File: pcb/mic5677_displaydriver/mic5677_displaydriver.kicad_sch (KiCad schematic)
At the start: 81 parts, among them J1 Segment DIP14, J2 Segment DIP14, J3 Segment Wire Connector, J4 Common Cathode Enable, J5 PSU, J6 Bypass, J7 Serial Debug, J8 8P8C, Q1 D45H8G, Q10 BC546, Q11 BC546, Q12 BC546, Q13 BC546, Q14 BC546, Q15 BC546, Q16 BC546, Q17 BC546, Q18 BC546, Q19 BC546, Q2 D45H8G, Q20 BC546, Q21 BC546, Q22 BC546, Q23 BC546, Q3 D45H8G, Q4 D45H8G, Q5 D45H8G, Q6 D45H8G, Q7 D45H8G, Q8 D45H8G, Q9 D45H8G, U1 L7805, U2 74HC595, U3 74HC595, U4 74HC02

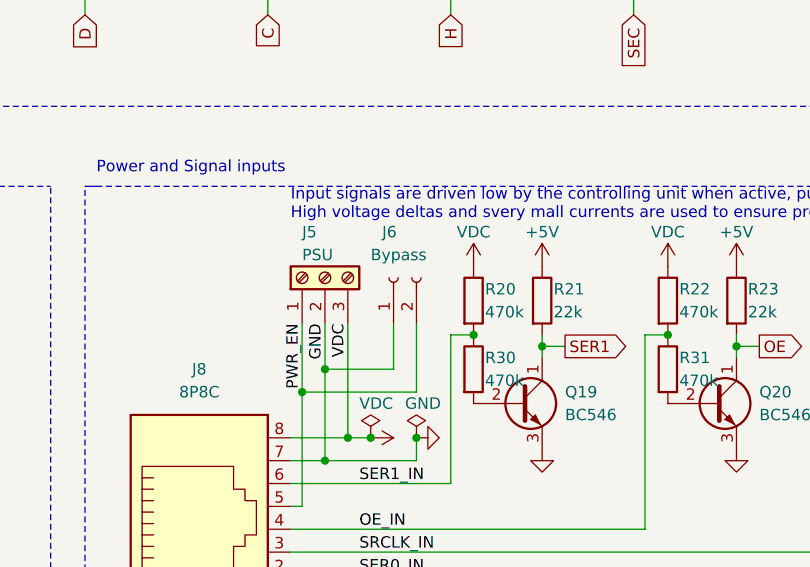
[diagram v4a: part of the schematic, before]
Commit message: Added some silkscreen on pcb and changed io style
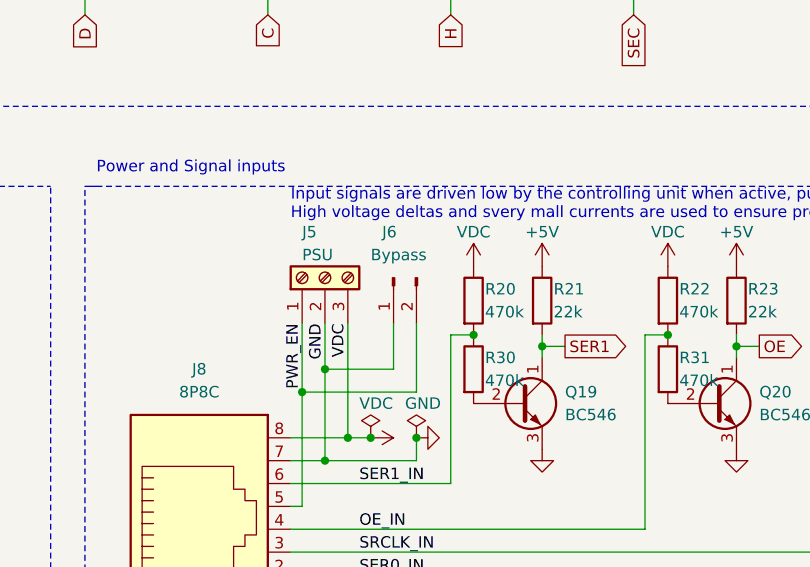
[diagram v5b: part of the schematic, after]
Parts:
- J6: symbol Connector:Conn_01x02_Socket -> Connector:Conn_01x02_Pin
- J7: footprint Connector_PinHeader_2.54mm:PinHeader_1x05_P2.54mm_Vertical -> Connector_PinSocket_2.54mm:PinSocket_1x05_P2.54mm_Vertical
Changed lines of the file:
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@@
       (effects (font (size 1.27 1.27)) (justify left))
     )
-    (property "Footprint" "Connector_PinHeader_2.54mm:PinHeader_1x05_P2.54mm_Vertical" (at 105.41 138.43 0)
+    (property "Footprint" "Connector_PinSocket_2.54mm:PinSocket_1x05_P2.54mm_Vertical" (at 105.41 138.43 0)
       (effects (font (size 1.27 1.27)) hide)
     )
@@
     )
   )
-  (symbol (lib_id "Connector:Conn_01x02_Socket") (at 166.37 114.3 90) (unit 1)
+  (symbol (lib_id "Connector:Conn_01x02_Pin") (at 166.37 114.3 90) (mirror x) (unit 1)
     (in_bom yes) (on_board yes) (dnp no)
     (property "Reference" "J6" (at 165.1 109.22 90)

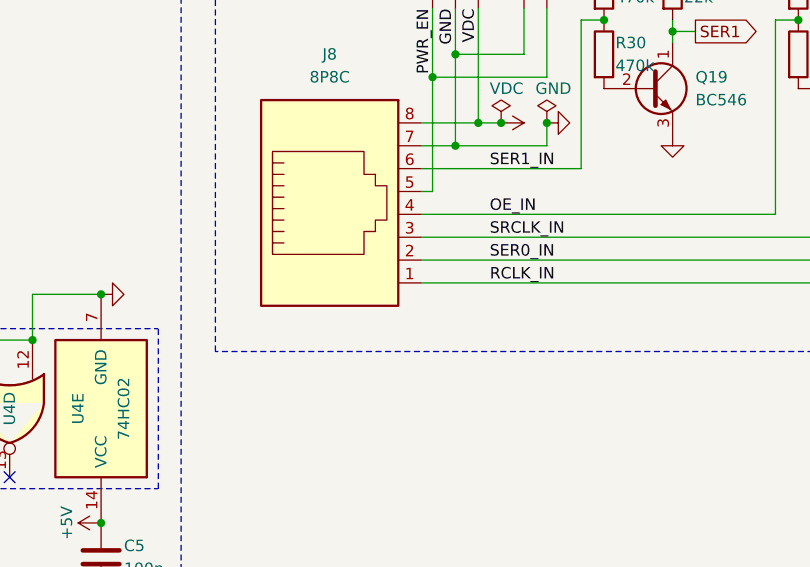
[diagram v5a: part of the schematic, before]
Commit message: Made display driver pcb work both with and without filled fill zones
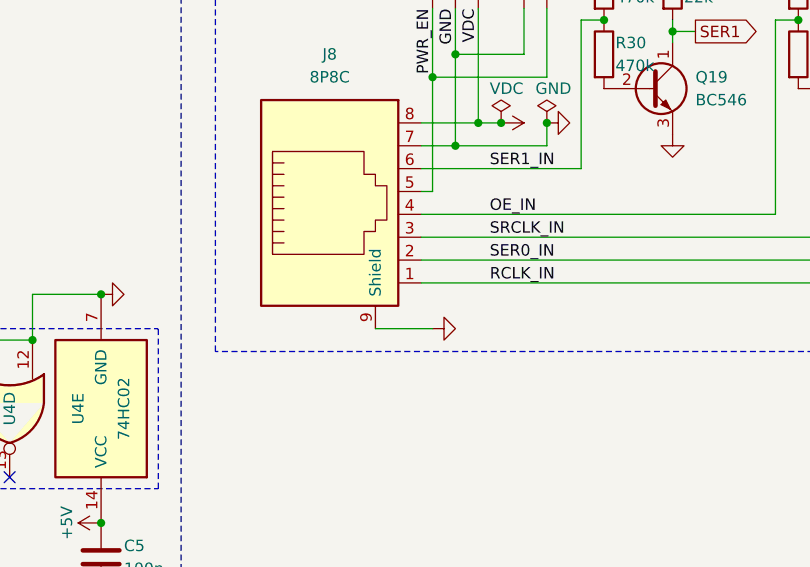
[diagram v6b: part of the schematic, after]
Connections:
- net GND: now also J8.9 (Shield)
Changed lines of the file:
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@@
+    (stroke (width 0) (type default))
+  )
+  (wire (pts (xy 149.86 154.94) (xy 156.21 154.94))
     (stroke (width 0) (type default))
   )
@@
     (pin "7")
     (pin "8")
+    (pin "9")
     (instances
       (project "mic5677_displaydriver"
@@
         )
       )
+    )
+  )
+  (symbol (lib_id "power:GND") (at 156.21 154.94 90) (unit 1)
+    (in_bom yes) (on_board yes) (dnp no) (fields_autoplaced)
+    (property "Reference" "#PWR030" (at 162.56 154.94 0)
+      (effects (font (size 1.27 1.27)) hide)
+    )
+    (property "Value" "GND" (at 160.02 154.94 90)
+      (effects (font (size 1.27 1.27)) (justify right) hide)
+    )
+    (property "Footprint" "" (at 156.21 154.94 0)
+      (effects (font (size 1.27 1.27)) hide)
+    )
+    (property "Datasheet" "" (at 156.21 154.94 0)
+      (effects (font (size 1.27 1.27)) hide)
+    )
+    (pin "1")
+    (instances
+      (project "mic5677_displaydriver"
+        (path "/904d3710-a02f-4e23-8828-29b05a2e6582"
+          (reference "#PWR030") (unit 1)
+        )
+      )

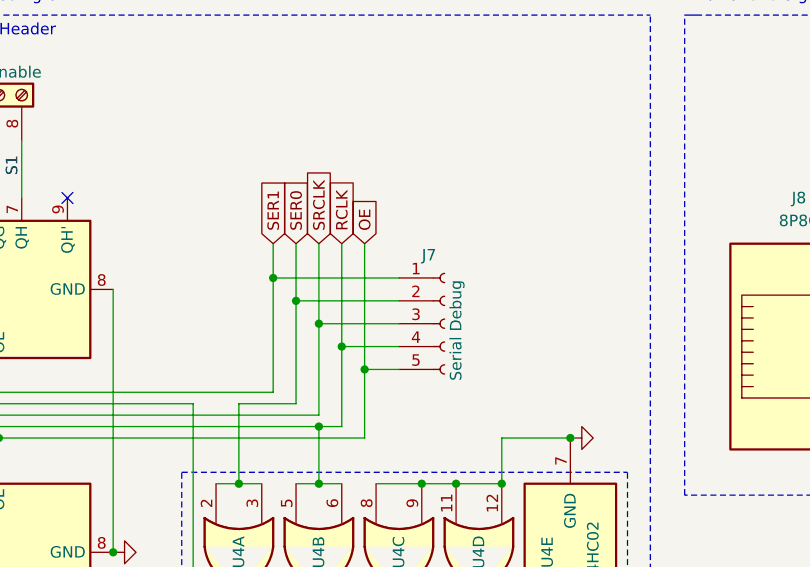
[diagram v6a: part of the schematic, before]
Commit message: Added power pins on serial debug port
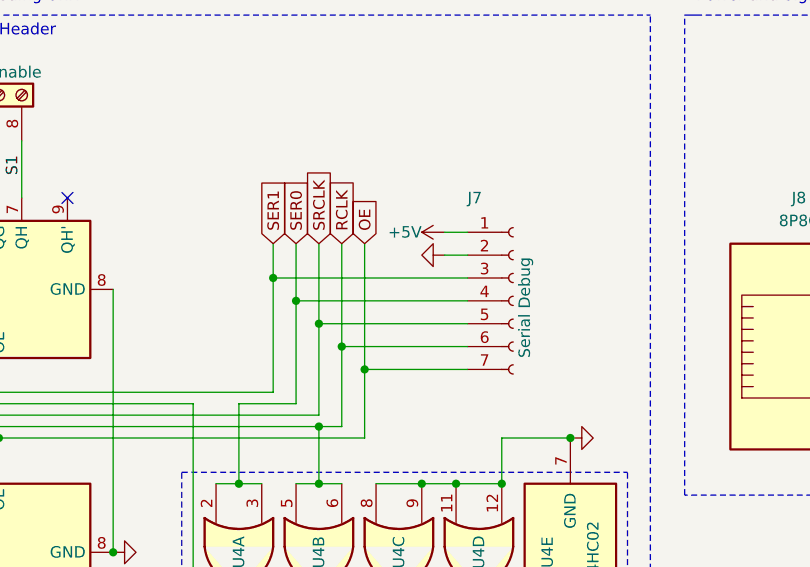
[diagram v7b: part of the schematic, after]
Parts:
- J7: footprint Connector_PinSocket_2.54mm:PinSocket_1x05_P2.54mm_Vertical -> Connector_PinSocket_2.54mm:PinSocket_1x07_P2.54mm_Vertical; symbol Connector:Conn_01x05_Socket -> Connector:Conn_01x07_Socket
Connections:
- net +5V: now also J7.1 (Pin_1)
- net GND: now also J7.2 (Pin_2)
- net OE: now also J7.7 (Pin_7); no longer J7.5 (Pin_5)
- net RCLK: now also J7.6 (Pin_6); no longer J7.4 (Pin_4)
- net SER0: now also J7.4 (Pin_4); no longer J7.2 (Pin_2)
- net SER1: now also J7.3 (Pin_3); no longer J7.1 (Pin_1)
- net SRCLK: now also J7.5 (Pin_5); no longer J7.3 (Pin_3)

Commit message: Updated ddriver to v2.3
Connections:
- net A_OUT: now also Q2.2 (C); no longer Q2.3 (E)
- net B_OUT: now also Q1.2 (C); no longer Q1.3 (E)
- net C_OUT: now also Q7.2 (C); no longer Q7.3 (E)
- net D_OUT: now also Q6.2 (C); no longer Q6.3 (E)
- net E_OUT: now also Q5.2 (C); no longer Q5.3 (E)
- net F_OUT: now also Q4.2 (C); no longer Q4.3 (E)
- net G_OUT: now also Q3.2 (C); no longer Q3.3 (E)
- net H_OUT: now also Q8.2 (C); no longer Q8.3 (E)
- net RCLK: now also R35.1
- net SEC_OUT: now also Q9.2 (C); no longer Q9.3 (E)
- net SRCLK: no longer R35.1
- net VDC: now also Q1.3 (E), Q2.3 (E), Q3.3 (E), Q4.3 (E), Q5.3 (E), Q6.3 (E), Q7.3 (E), Q8.3 (E), Q9.3 (E); no longer Q1.2 (C), Q2.2 (C), Q3.2 (C), Q4.2 (C), Q5.2 (C), Q6.2 (C), Q7.2 (C), Q8.2 (C), Q9.2 (C)
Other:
- note removed: "2.0"
- note removed: "2023-07-06"
- note removed: "Mictronic 5677 Scoreboard - Head Display Control Unit"
- title: (none) -> Mictronic 5677 Scoreboard - Head Display Control Unit
- moved on the sheet: D2, R35
